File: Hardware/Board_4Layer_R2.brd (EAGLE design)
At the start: 101.3 x 45.7 mm, 54 parts, among them U1 EDISON_CONNECTOR_FULLMOUNTING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, U2 LAN9512-JZX, U3 MAX4995AAUT+, U4 EDISON_CONNECTOR_FULLHEADER, X1 J1011F01P

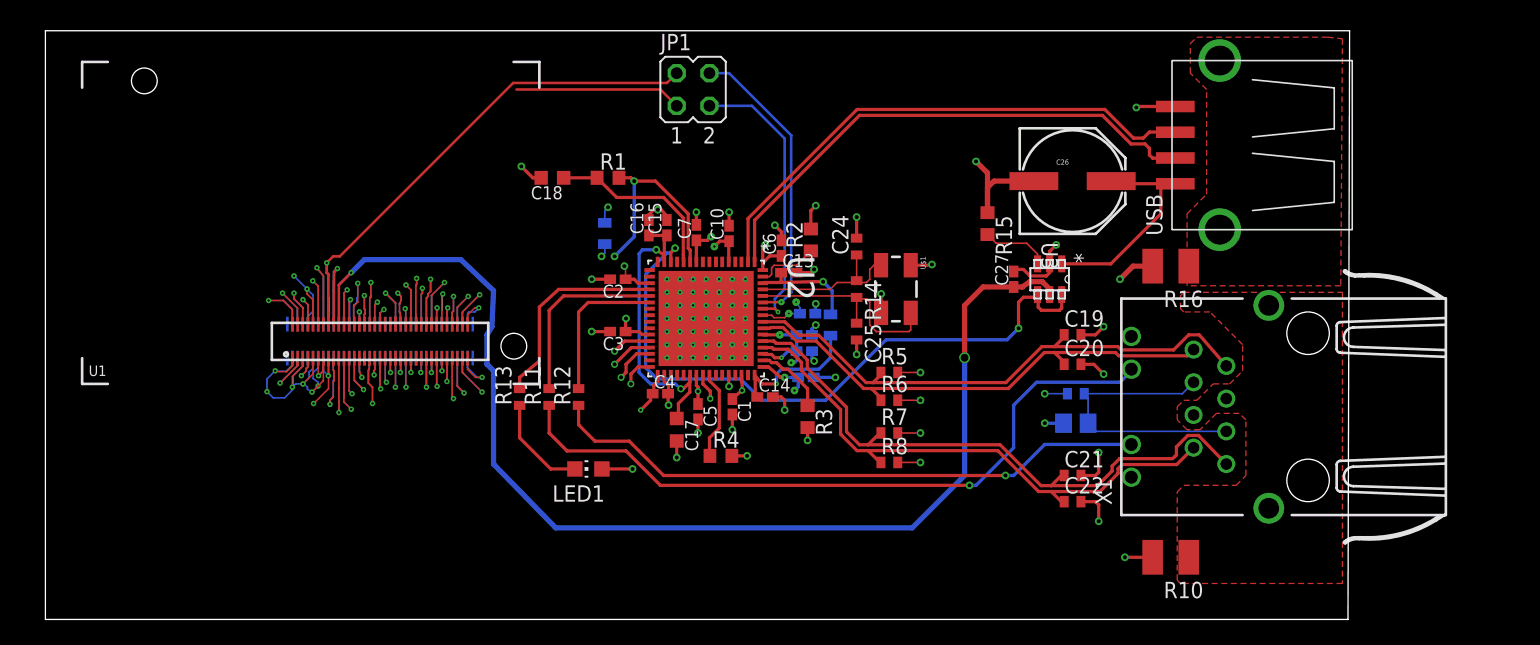
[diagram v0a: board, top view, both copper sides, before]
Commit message: Finished first board layout Board_4layer_R2
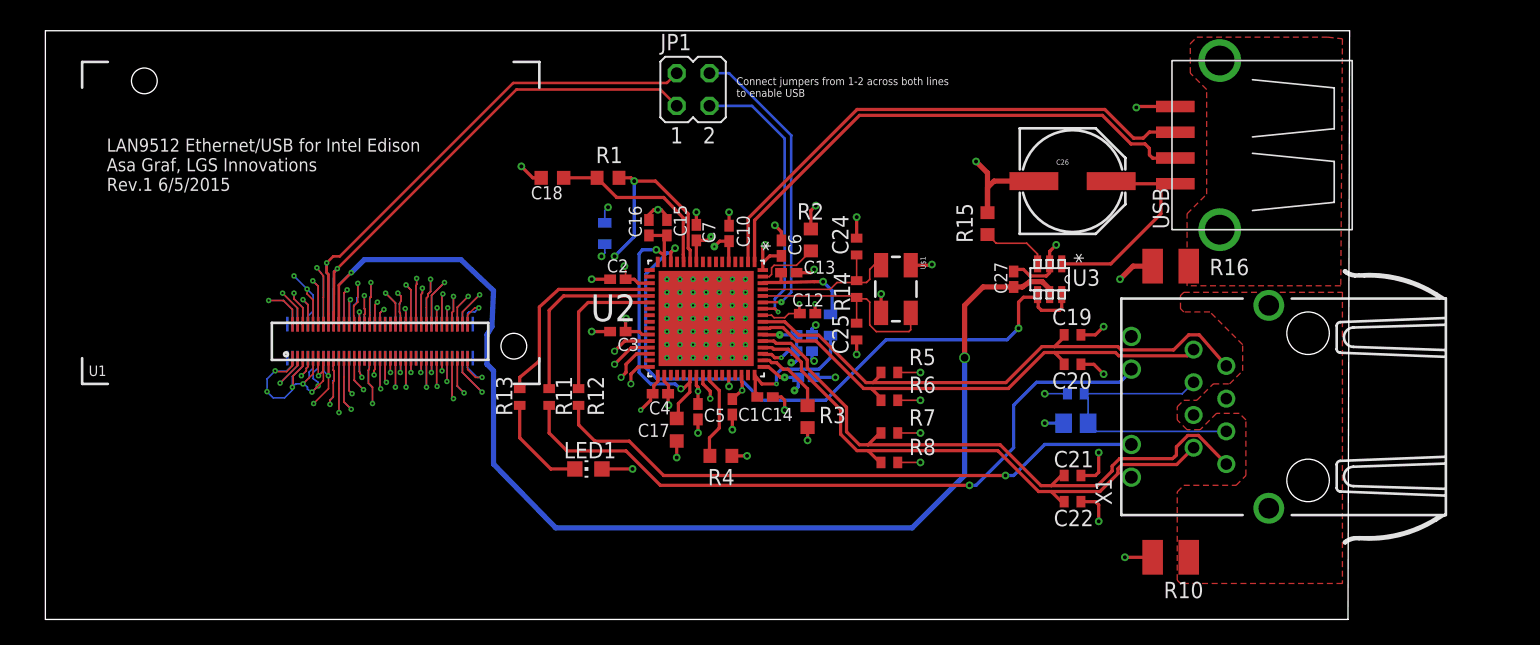
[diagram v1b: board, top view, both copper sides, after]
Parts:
- flipped C12 to the top, turned to 0 degrees
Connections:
- removed net S$1: U1.18, U4.18
- net USBUPN: now also U1.18, U4.18
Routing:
- net USBUPN: track 13.0 -> 41.5 mm, vias 0 -> 1
- net S$1: track 8.85 -> 0.00 mm, vias 1 -> 0
- net VDD33A: track 36.3 -> 36.1 mm, vias 16 -> 15
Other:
- board text added: "Connect jumpers from 1-2 across both lines to enable USB"
- board text added: "LAN9512 Ethernet/USB for Intel Edison Asa Graf, LGS Innovations Rev.1 6/5/2015"

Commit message: Updated board and schematic as per recommendations.
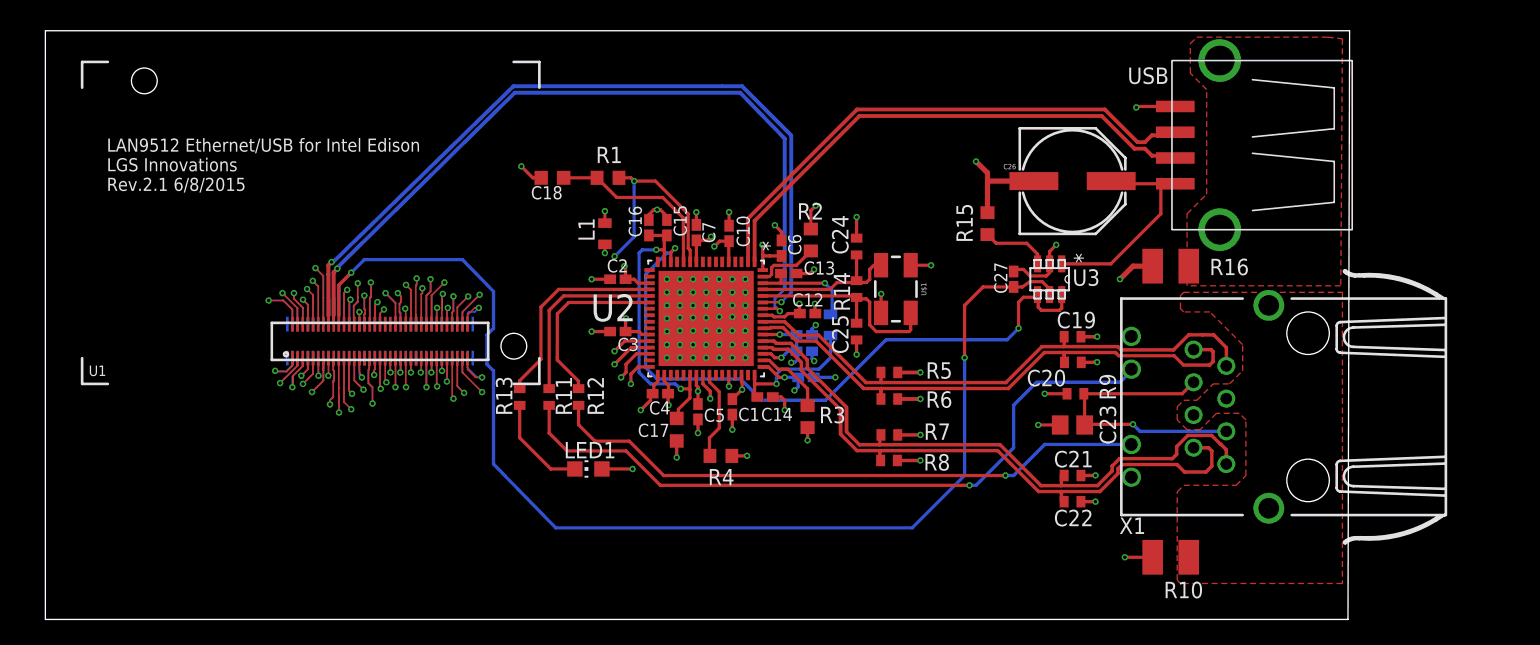
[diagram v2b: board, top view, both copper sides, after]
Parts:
- removed JP1: (no value), jumper:JP2Q
- moved C23 0.30 mm to (80.0, 15.1), flipped to the top, turned to 180 degrees
- moved R8 0.15 mm to (65.8, 12.3)
- moved C20 0.15 mm to (80.0, 20.0)
- moved R7 0.15 mm to (65.8, 14.3)
- moved C19 0.15 mm to (80.0, 21.9)
- moved R6 0.10 mm to (65.8, 17.1)
- moved C13 0.06 mm to (58.0, 26.9)
- flipped R9 to the top, turned to 180 degrees
- flipped L1 to the top
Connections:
- removed net USBUP: JP1.3, U1.16, U4.16
- removed net USBUPDN: JP1.2, U2.58
- removed net USBUPDP: JP1.4, U2.59
- removed net USBUPN: JP1.1, U1.18, U4.18
- new net USBUP_N: U1.18, U2.58, U4.18
- new net USBUP_P: U1.16, U2.59, U4.16
- net GND: no longer U2.65
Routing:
- net USBUP_P: track 0.00 -> 67.4 mm, vias 0 -> 2
- net USBUP_N: track 0.00 -> 66.0 mm, vias 0 -> 2
- net USBUP: track 42.9 -> 0.00 mm, vias 1 -> 0
- net USBUPN: track 41.5 -> 0.00 mm, vias 1 -> 0
- net USBUPDP: track 23.1 -> 0.00 mm, vias 1 -> 0
- net USBUPDN: track 22.1 -> 0.00 mm, vias 1 -> 0
- net GND: track 108.4 -> 89.0 mm, vias 92 -> 53
- net RX_N: track 43.9 -> 47.3 mm
- net TX_P: track 39.4 -> 42.6 mm
- net N$18: track 11.8 -> 14.0 mm
- net VDD3IO: track 113.6 -> 111.4 mm, vias 18 -> 17
- net N$4: track 23.9 -> 23.1 mm
- net N$2: track 11.3 -> 10.7 mm
- net VDD33A: track 36.1 -> 35.5 mm
- net N$10: track 22.3 -> 22.6 mm, vias 0 -> 1
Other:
- board text added: "LAN9512 Ethernet/USB for Intel Edison LGS Innovations Rev.2.1 6/8/2015"
- board text removed: "Connect jumpers from 1-2 across both lines to enable USB"
- board text removed: "LAN9512 Ethernet/USB for Intel Edison Asa Graf, LGS Innovations Rev.1 6/5/2015"

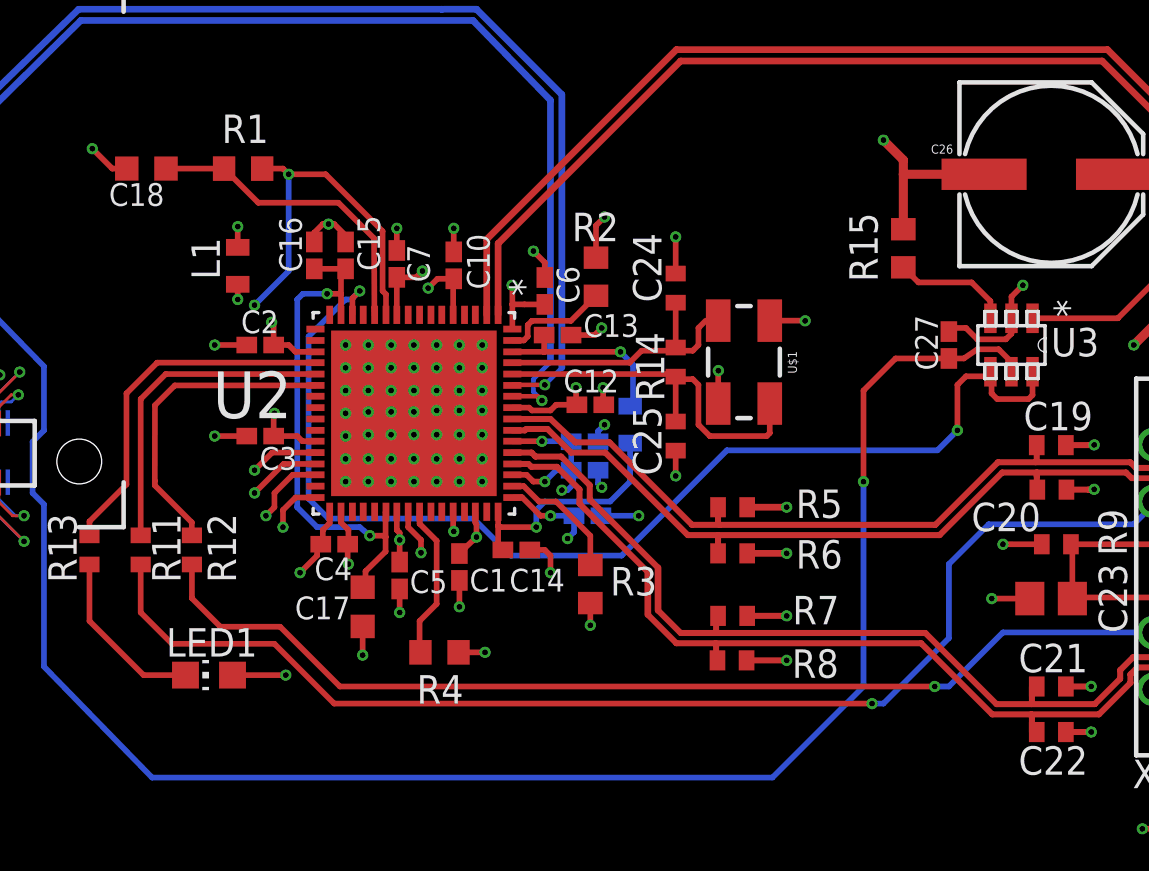
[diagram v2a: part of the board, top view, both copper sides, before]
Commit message: Removed olf board file, made some changes to new board file and schematic. BOM is till complete.
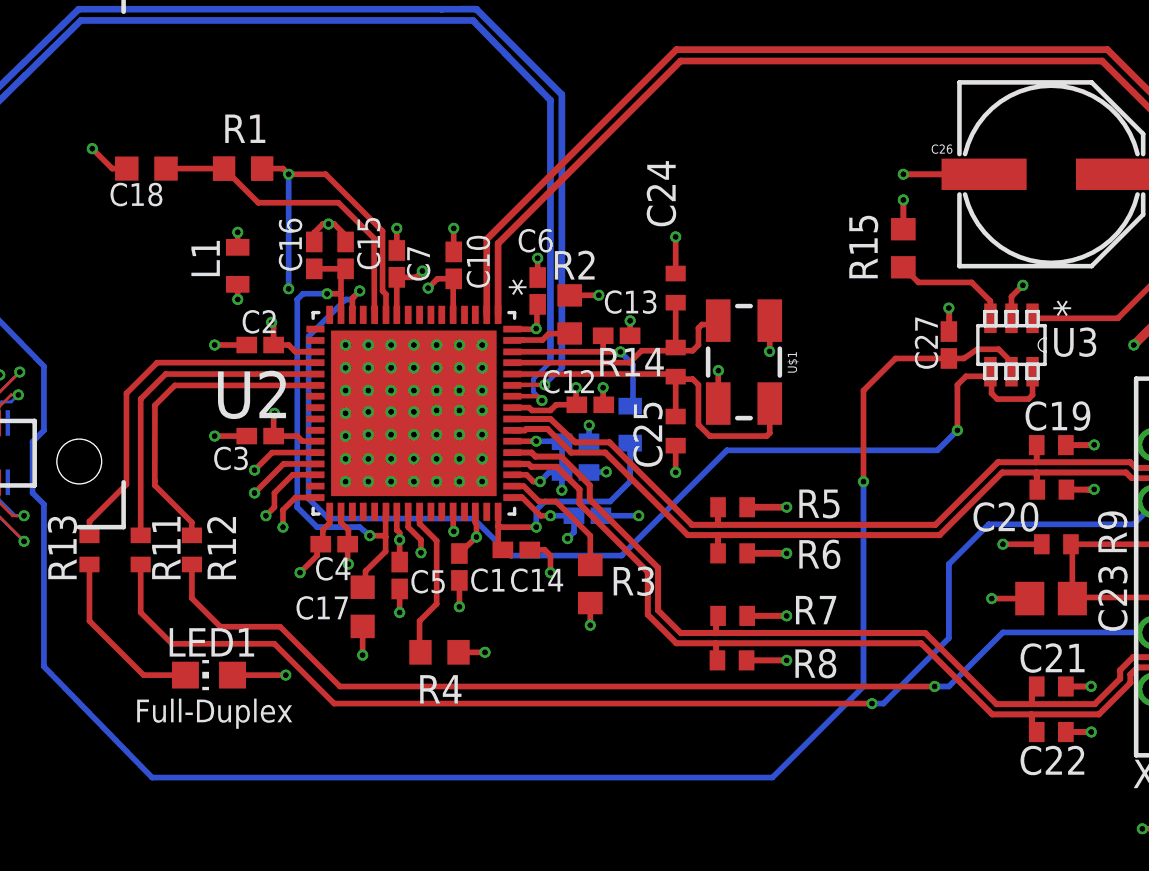
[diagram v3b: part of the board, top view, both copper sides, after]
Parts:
- moved C13 2.64 mm to (60.6, 26.8)
- moved R2 2.05 mm to (58.5, 27.8)
- moved C9 0.42 mm to (58.8, 20.7)
- moved C11 0.41 mm to (58.8, 22.1)
- moved C6 0.32 mm to (57.1, 28.8)
- moved C25 0.22 mm to (63.2, 22.6)
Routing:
- net GND: track 89.0 -> 80.9 mm, vias 53 -> 91
- net N$6: track 4.86 -> 2.68 mm
- net VDD33A: track 35.5 -> 33.7 mm
- net VDD3IO: track 111.4 -> 110.0 mm
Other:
- board text added: "Full-Duplex"

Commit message: Revised board.
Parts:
- moved C16 14.4 mm to (48.8, 16.1), turned to 270 degrees
- moved R13 1.75 mm to (37.1, 15.5)
- moved C17 1.61 mm to (49.9, 16.2)
- moved R11 1.21 mm to (39.4, 18.5)
- moved U$1 0.99 mm to (66.4, 26.6)
- moved C14 0.94 mm to (55.3, 16.8), turned to 270 degrees
- moved C4 0.77 mm to (47.5, 16.9), turned to 270 degrees
- moved C1 0.70 mm to (54.3, 16.6)
- moved R12 0.67 mm to (41.7, 16.6)
- moved C15 0.43 mm to (48.3, 30.0)
- moved C11 0.38 mm to (58.4, 22.1)
- moved C9 0.36 mm to (58.5, 20.5)
- moved C12 0.19 mm to (59.4, 23.9)
- moved C5 0.10 mm to (51.0, 16.1)
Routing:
- net GND: track 80.9 -> 66.9 mm, vias 91 -> 92
- net VDD33A: track 33.7 -> 30.5 mm
- net VDD3IO: track 110.0 -> 107.9 mm
- net N$20: track 16.0 -> 17.8 mm
- net N$19: track 7.81 -> 6.06 mm
- net N$4: track 23.1 -> 21.6 mm
- net N$2: track 10.7 -> 12.1 mm
- net N$16: track 54.8 -> 56.0 mm
- net N$15: track 14.3 -> 13.1 mm
- net N$21: track 12.5 -> 13.6 mm
- net N$22: track 16.8 -> 15.8 mm
- net N$17: track 47.1 -> 46.4 mm
- net N$18: track 14.0 -> 14.7 mm
- net N$7: track 14.0 -> 14.6 mm
- net N$10: vias 1 -> 0

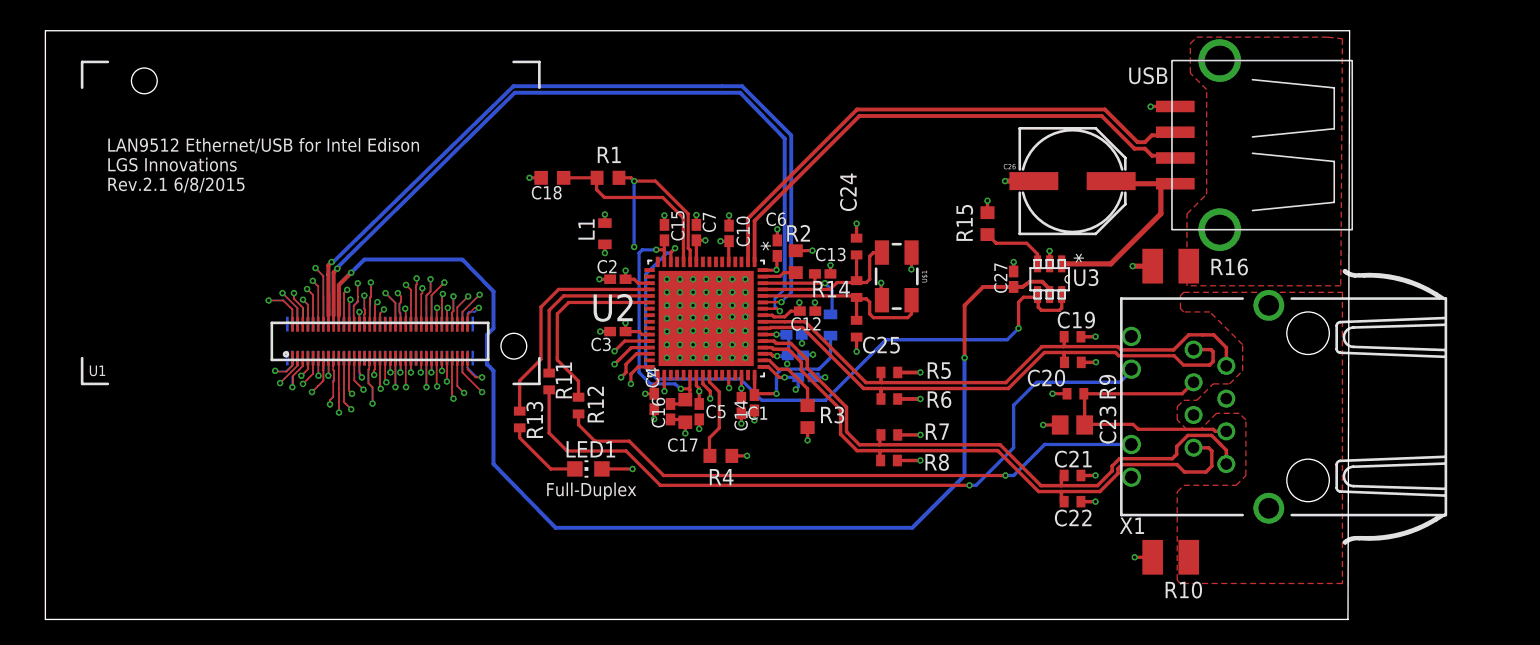
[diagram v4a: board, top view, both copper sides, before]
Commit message: Board ready for manufacturing: Added mounting hardware and verified trace impedances. Designed to Advanced Circuit's specifications and passes their checks at FreeDFM.com.
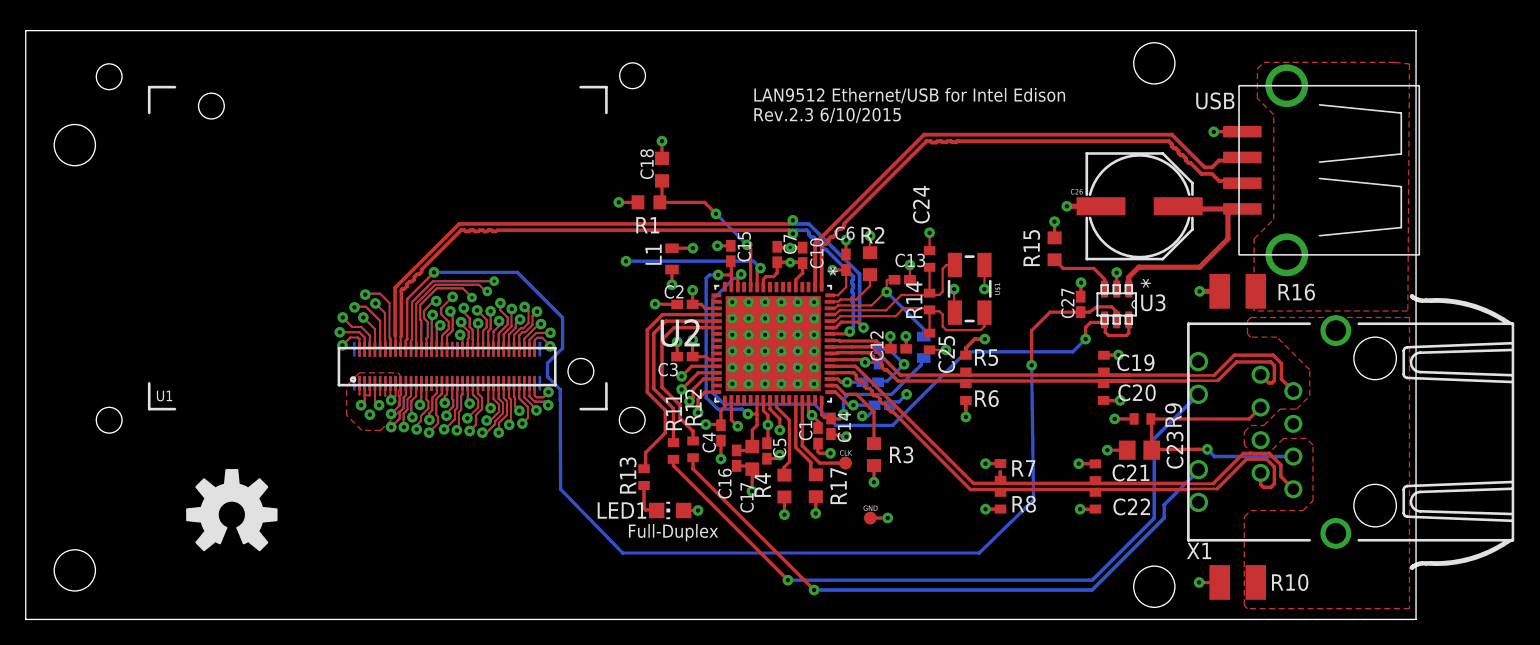
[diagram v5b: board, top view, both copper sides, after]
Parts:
- added CLK_PAD: CLK, testpad:TP10R
- added E$2: (no value), SparkFun-Aesthetics:OSHW-LOGO-L
- added GNDPAD: GNDPAD, testpad:TP10R
- added R17: 10K, resistor:R0603
- moved R11 11.1 mm to (49.0, 13.1)
- moved R13 10.6 mm to (46.7, 11.0)
- moved R12 9.52 mm to (50.5, 13.2)
- moved R8 9.20 mm to (74.4, 9.22), turned to 270 degrees
- moved R7 9.10 mm to (74.4, 11.5), turned to 90 degrees
- moved C18 8.53 mm to (48.1, 34.9), turned to 90 degrees
- moved C12 7.65 mm to (66.5, 21.0)
- moved L2 7.44 mm to (68.5, 21.1)
- moved LED1 7.12 mm to (48.8, 8.46)
- moved C11 6.75 mm to (64.9, 20.5), turned to 90 degrees
- moved C7 6.50 mm to (57.1, 28.3)
- moved C1 6.41 mm to (60.2, 14.2)
- moved C17 6.35 mm to (55.1, 12.5)
- moved C8 6.30 mm to (65.2, 16.6)
- moved C16 6.27 mm to (53.9, 12.5)
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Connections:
- removed net P3: U1.3, U4.3
- removed net P68: U1.68, U4.68
- new net CLKOUT: CLK_PAD.TP, U2.45
- new net S$4: R17.1, U2.44
- new net S$5: U4.70
- new net S$6: U4.20
- new net S$7: U4.68
- new net S$8: U1.68
- net GND: now also GNDPAD.TP, U1.3, U4.3; no longer U2.44
- net P70: no longer U4.70
- net USB_VBUS: no longer U4.20
- net VDD3IO: now also R17.2
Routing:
- net P22: track 5.55 -> 21.5 mm
- net P24: track 3.90 -> 19.8 mm
- net USBUP_N: track 66.0 -> 50.6 mm
- net USBUP_P: track 67.4 -> 52.3 mm
- net P26: track 6.63 -> 16.6 mm
- net GP28_I2C_6_SDA: track 0.00 -> 7.63 mm, vias 0 -> 1
- net VDD33A: track 30.5 -> 38.1 mm, vias 15 -> 13
- net CLKOUT: track 0.00 -> 7.44 mm
- net P55: track 2.22 -> 9.36 mm
- net P28: track 1.91 -> 8.95 mm
- net VDD3IO: track 107.9 -> 114.6 mm, vias 17 -> 19
- net S$4: track 0.00 -> 6.68 mm
- net P34: track 3.60 -> 9.89 mm
- net P62: track 2.59 -> 8.08 mm
- net P33: track 2.63 -> 8.06 mm
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- added copper zone on layer 1, net GND
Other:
- board size 101.3 x 45.7 mm -> 108 x 45.7 mm
- board text added: "CLK"
- board text added: "Designed By: Asa Graf"
- board text added: "GND"
- board text added: "LAN9512 Ethernet/USB for Intel Edison Rev.2.3 6/10/2015"
- board text removed: "LAN9512 Ethernet/USB for Intel Edison LGS Innovations Rev.2.1 6/8/2015"
